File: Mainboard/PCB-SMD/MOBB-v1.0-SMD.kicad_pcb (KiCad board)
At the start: 2 copper layers, 85.6 x 49.7 mm, 153 parts, among them P1 AUX 1-3, P14 EXTRA Pins, P2 VUSB, P3 +3.3V, P4 Pit Limiter, P5 Rotary Encoders, P6 BTN 1-32, P7 LED, Q1 NPN, Q2 NPN, Q3 NPN, Q4 NPN, U1 74HC4051, U2 74HC4051, U3 74HC4051, U4 74HC4051, U5 Teensy3.2

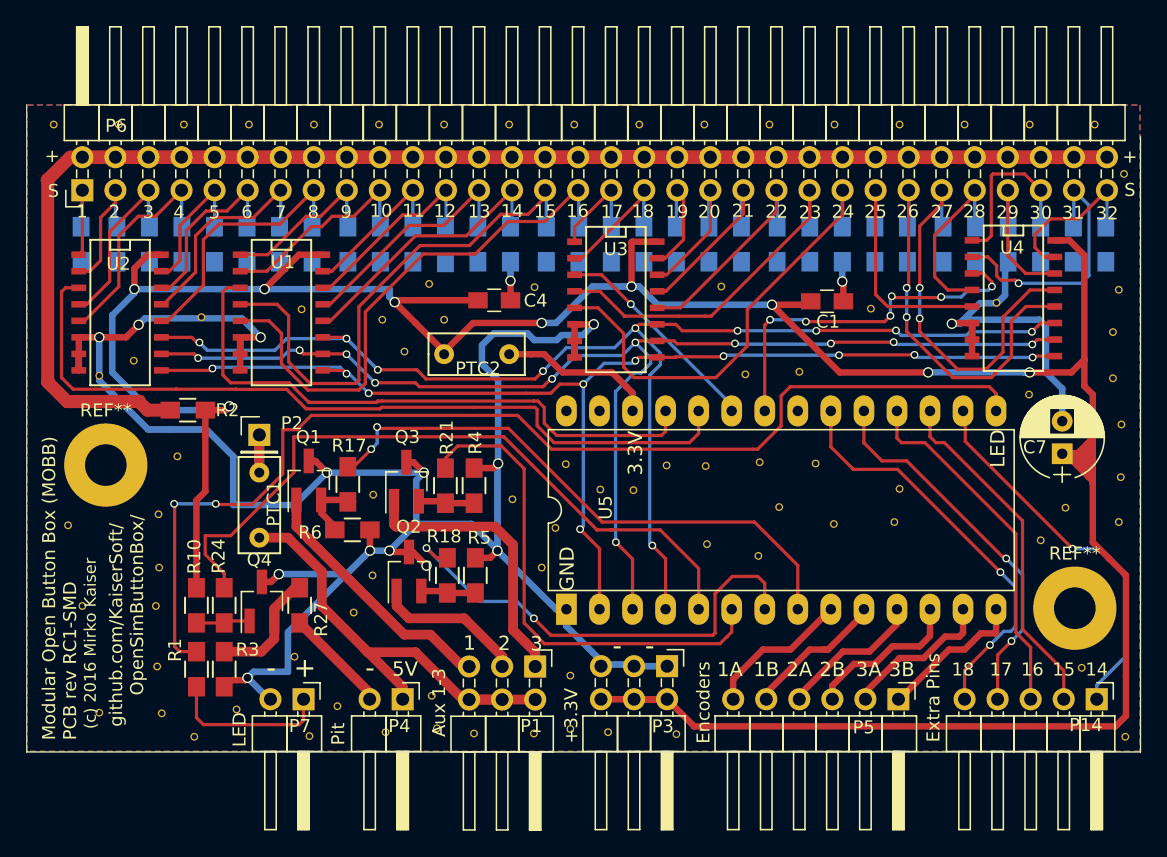
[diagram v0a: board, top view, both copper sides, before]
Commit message: * moved all components to top side to allow for cheaper manufcaturing * rearanged multiplexers to make room for bottom resistors
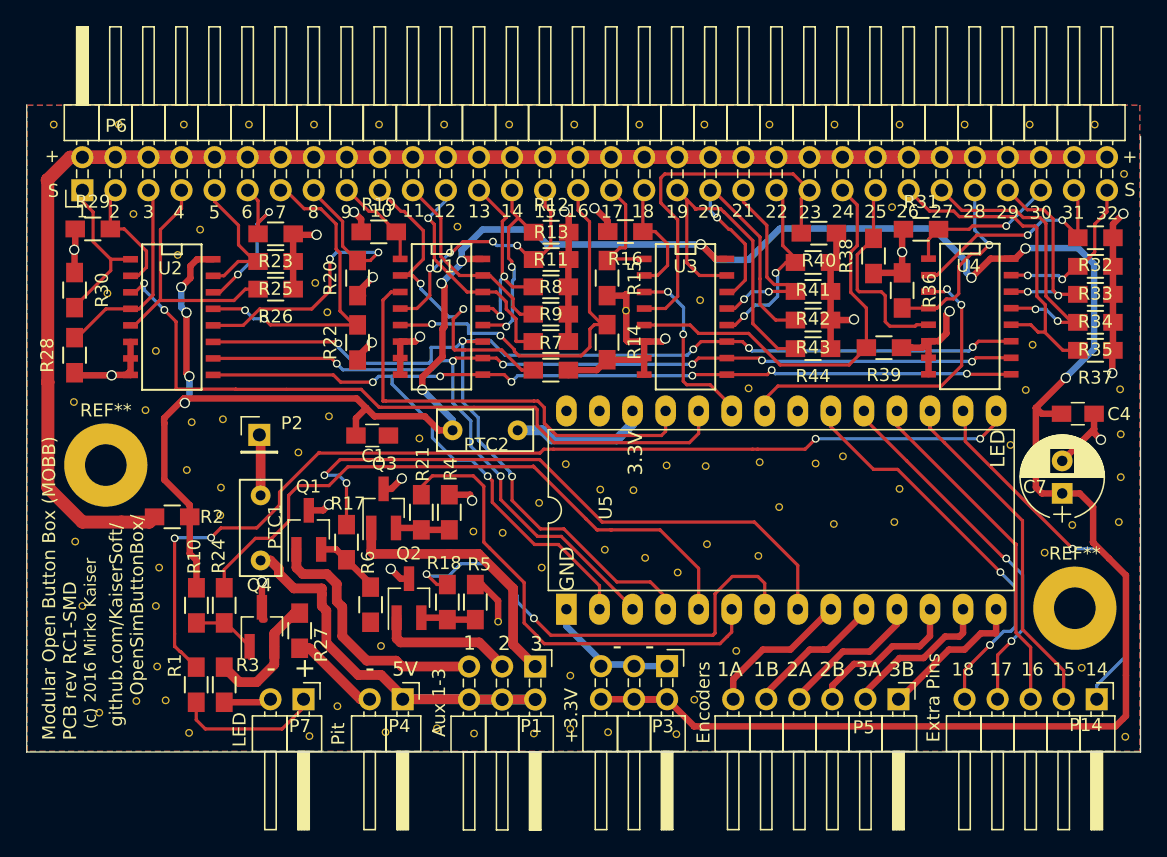
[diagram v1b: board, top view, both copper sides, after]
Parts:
- added Ref**: Val**, MOBB-KiCad-Lib:VIA-W0.6mm-H0.4mm, F.Cu at (225.3, 131.0)
- added Ref**: Val**, MOBB-KiCad-Lib:VIA-W0.6mm-H0.4mm, F.Cu at (226.6, 140.8)
- added Ref**: Val**, MOBB-KiCad-Lib:VIA-W0.6mm-H0.4mm, F.Cu at (219.8, 129.2)
- added Ref**: Val**, MOBB-KiCad-Lib:VIA-W0.6mm-H0.4mm, F.Cu at (214.7, 125.6)
- added Ref**: Val**, MOBB-KiCad-Lib:VIA-W0.6mm-H0.4mm, F.Cu at (222.8, 129.8)
- added Ref**: Val**, MOBB-KiCad-Lib:VIA-W0.6mm-H0.4mm, F.Cu at (208.4, 104.4)
- added Ref**: Val**, MOBB-KiCad-Lib:VIA-W0.6mm-H0.4mm, F.Cu at (250.9, 121.2)
- added Ref**: Val**, MOBB-KiCad-Lib:VIA-W0.6mm-H0.4mm, F.Cu at (197.5, 108.7)
- added Ref**: Val**, MOBB-KiCad-Lib:VIA-W0.6mm-H0.4mm, F.Cu at (183.5, 103.4)
- added Ref**: Val**, MOBB-KiCad-Lib:VIA-W0.6mm-H0.4mm, F.Cu at (229.8, 137.0)
- R11, R12, R13, R14, R15, R16, R19, R20, R22, R23, R25, R26, R28, R29, R30, R31, R32, R33, R34, R35, R36, R37, R38, R39, R40, R41, R42, R43, R44, R7, R8, R9: moved to F.Cu
- moved Ref** 48.6 mm to (186.9, 106.6)
- moved C4 45.7 mm to (256.1, 118.8)
- moved Ref** 37.5 mm to (221.4, 110.8)
- moved C1 36.4 mm to (201.9, 120.5)
- moved Ref** 26.0 mm to (205.5, 120.7)
- moved Ref** 19.0 mm to (187.6, 123.1)
- moved Ref** 18.7 mm to (184.4, 118.5)
- moved Ref** 18.1 mm to (188.7, 104.6)
- moved R37 16.6 mm to (257.4, 113.9), turned to 180 degrees
- moved R7 16.3 mm to (215.6, 115.4), turned to 0 degrees
- moved Ref** 15.7 mm to (196.2, 121.8)
- moved Ref** 14.9 mm to (190.4, 119.2)
- moved R44 13.2 mm to (235.8, 113.8), turned to 180 degrees
- moved Ref** 13.2 mm to (190.2, 124.5)
- moved R35 13.1 mm to (257.4, 111.8), turned to 180 degrees
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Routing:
- net GND: track 197.9 -> 127.8 mm, vias 16 -> 21
- net +3V3: track 239.2 -> 216.6 mm, vias 9 -> 11
- net Net-(P6-Pad29): track 40.6 -> 21.1 mm, vias 0 -> 4
- net Net-(P6-Pad37): track 9.44 -> 27.1 mm
- net Net-(P6-Pad39): track 11.5 -> 23.8 mm, vias 0 -> 1
- net Net-(U1-Pad3): track 46.4 -> 34.6 mm
- net Net-(P6-Pad31): track 41.9 -> 30.9 mm, vias 0 -> 2
- net Net-(P6-Pad19): track 16.1 -> 26.1 mm, vias 0 -> 2
- net Net-(P6-Pad13): track 17.3 -> 25.5 mm, vias 0 -> 2
- net Net-(R1-Pad1): track 87.0 -> 79.1 mm, vias 2 -> 4
- net PINHEADERSRC: track 268.2 -> 275.3 mm
- net Net-(U2-Pad3): track 62.0 -> 55.1 mm, vias 0 -> 2
- net Net-(P6-Pad27): track 21.6 -> 14.9 mm, vias 0 -> 2
- net Net-(P6-Pad53): track 30.1 -> 23.5 mm
- net Net-(U1-Pad10): track 95.0 -> 88.6 mm, vias 11 -> 7
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
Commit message: * final tweaks to MainBoard SMD RC1 release. this is for testing only at this point
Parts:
- added Ref**: Val**, MOBB-KiCad-Lib:VIA-W0.6mm-H0.4mm, F.Cu at (228.2, 138.5)
- added Ref**: Val**, MOBB-KiCad-Lib:VIA-W0.6mm-H0.4mm, F.Cu at (181.3, 114.1)
- added Ref**: Val**, MOBB-KiCad-Lib:VIA-W0.6mm-H0.4mm, F.Cu at (190.3, 129.4)
- added Ref**: Val**, MOBB-KiCad-Lib:VIA-W0.6mm-H0.4mm, F.Cu at (230.0, 130.2)
- moved Ref** 22.9 mm to (220.0, 129.1)
- moved Ref** 5.95 mm to (196.3, 120.0)
- moved Ref** 4.78 mm to (215.9, 126.3)
- moved Ref** 4.77 mm to (242.1, 124.5)
- moved Ref** 2.20 mm to (211.6, 128.8)
- moved Ref** 2.17 mm to (209.8, 127.4)
- moved Ref** 2.14 mm to (185.2, 142.8)
- moved Ref** 2.11 mm to (188.4, 121.2)
- moved Ref** 2.08 mm to (190.1, 119.5)
- moved Ref** 1.57 mm to (232.8, 130.7)
- moved Ref** 1.45 mm to (216.3, 131.1)
- moved Ref** 1.43 mm to (188.9, 123.9)
- moved Ref** 1.38 mm to (227.0, 124.1)
- moved Ref** 1.25 mm to (230.4, 122.3)
- moved Ref** 1.07 mm to (214.1, 124.8)
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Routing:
- net Net-(R21-Pad2): track 36.7 -> 34.7 mm
- net Net-(R18-Pad2): track 37.3 -> 35.8 mm
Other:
- board size 85.6 x 49.7 mm -> 85.6 x 49.8 mm
